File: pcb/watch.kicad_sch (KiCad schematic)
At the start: 18 parts, among them U1 nRF52840, Y1 Crystal

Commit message: sussy
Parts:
- added C17, C18: 12pF, symbol Device:C_Small
- added D10, D11, D9: D_TVS, symbol Device:D_TVS
- added F2: 1A/1.8A, Fuse:Fuse_1206_3216Metric_Pad1.42x1.75mm_HandSolder, symbol Device:Polyfuse_Small
- added J1: USB_C_Receptacle_USB2.0_14P, Connector_USB:USB_C_Receptacle_G-Switch_GT-USB-7010ASV, symbol Connector:USB_C_Receptacle_USB2.0_14P
- added L3: 10uH, symbol Device:L_Small
- added R17, R18: 5.1k, Resistor_SMD:R_0603_1608Metric_Pad0.98x0.95mm_HandSolder, symbol Device:R_Small
- added Y2: 32.768KHz, symbol Device:Crystal
- Y1: value Crystal -> 32MHz
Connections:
- net GND: now also C10.1, C11.1, C17.1, C18.1, D10.1 (A1), D11.1 (A1), D9.1 (A1), J1.A1 (GND), J1.A12 (GND), J1.B1 (GND), J1.B12 (GND), J1.S1 (SHIELD), R17.2, R18.2
- net VBUS: now also D11.2 (A2), F2.2
- net at C11.2: now also U1.A23 (XC2), Y1.1
- net at Y1.2: now also C10.2, U1.B24 (XC1)
- net VDD_nRF: now reaches C3.1, C4.1, C5.1, C6.1, C7.1, U1.A22 (VDD), U1.AD14 (VDD), U1.AD23 (VDD), U1.B1 (VDD), U1.W1 (VDD)
- net VDD_nRF: now also L3.1
- net at U1.AB2 (DCCH): now also L3.2
- net P0.16: now reaches U1.AC11 (P0.16)
- net P0.25: now reaches U1.AC21 (P0.25)
- net P0.14: now reaches U1.AC9 (P0.14)
- net P0.15: now reaches U1.AD10 (P0.15)
- net D-: now reaches U1.AD4 (D-)
- net D-: now also D10.2 (A2), J1.A7 (D-), J1.B7 (D-)
- net D+: now reaches U1.AD6 (D+)
- net D+: now also D9.2 (A2), J1.A6 (D+), J1.B6 (D+)
- net P0.13: now reaches U1.AD8 (P0.13)
- net at U1.D2 (XL1/P0.00): now also C18.2, Y2.1
- net at U1.F2 (XL2/P0.01): now also C17.2, Y2.2
- net P0.26: now reaches U1.G1 (P0.26)
- net P1.06: now reaches U1.R24 (P1.06)
- net P1.05: now reaches U1.T23 (P1.05)
- net P1.04: now reaches U1.U24 (P1.04)
- new net: J1.B5 (CC2), R18.1
- new net: J1.A5 (CC1), R17.1
- new net: F2.1, J1.A4 (VBUS), J1.A9 (VBUS), J1.B4 (VBUS), J1.B9 (VBUS)
- no-connect marks 5 -> 9
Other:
- moved on the sheet: C10, C11, C12, C13, C14, C15, C2, C3, C4, C5, C6, C7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

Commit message: stuff
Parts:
- added SW1, SW2, SW3, SW4: SW_Push, symbol Switch:SW_Push
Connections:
- net GND: now also SW1.2, SW2.2, SW3.2, SW4.2
- net P1.13: now reaches U1.A16 (P1.13)
- net P1.10: now reaches U1.A20 (P1.10)
- net P1.14: now reaches U1.B15 (P1.14)
- net P1.12: now reaches U1.B17 (P1.12)
- net P1.11: now reaches U1.B19 (P1.11)
- net P1.07: now reaches U1.P23 (P1.07)
- net P1.07: now also SW4.1
- net P1.03: now reaches U1.V23 (P1.03)
- net P1.03: now also SW3.1
- net P1.02: now reaches U1.W24 (P1.02)
- net P1.02: now also SW2.1
- net P1.01: now reaches U1.Y23 (P1.01)
- net P1.01: now also SW1.1
- no-connect marks 9 -> 14
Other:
- moved on the sheet: D10, D11, D9, F2, J1, R17, R18

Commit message: sus commit
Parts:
- removed D10, D11, D9: D_TVS, symbol Device:D_TVS
- added U9: USBLC6-2SC6, Package_TO_SOT_SMD:SOT-23-6, symbol Power_Protection:USBLC6-2SC6
- C10, C11, C17, C18: footprint (none) -> Capacitor_SMD:C_0402_1005Metric; LCSC Part (none) -> C1547
- C12: footprint (none) -> Capacitor_SMD:C_0402_1005Metric; LCSC Part (none) -> C52923
- C13: footprint (none) -> Capacitor_SMD:C_0603_1608Metric; LCSC Part (none) -> C1622
- C14: footprint (none) -> Capacitor_SMD:C_0402_1005Metric; LCSC Part (none) -> C1546
- C15, C7, C8, C9: footprint (none) -> Capacitor_SMD:C_0603_1608Metric; LCSC Part (none) -> C19666
- C2, C3, C4, C5, C6: footprint (none) -> Capacitor_SMD:C_0402_1005Metric; LCSC Part (none) -> C1525
- L1, L3: footprint (none) -> Inductor_SMD:L_0805_2012Metric; LCSC Part (none) -> C88182
- L2: footprint (none) -> Inductor_SMD:L_0402_1005Metric; LCSC Part (none) -> C98055
- R17, R18: value 5.1k -> 4.12k; footprint Resistor_SMD:R_0603_1608Metric_Pad0.98x0.95mm_HandSolder -> Resistor_SMD:R_0402_1005Metric; LCSC Part C23186 -> C2930007
- SW1, SW2, SW3, SW4: value SW_Push -> 10k; footprint (none) -> Resistor_SMD:R_0402_1005Metric; LCSC Part (none) -> C25744
- U1: value nRF52840 -> 5.1k; footprint Package_DFN_QFN:Nordic_AQFN-73-1EP_7x7mm_P0.5mm -> Resistor_SMD:R_0603_1608Metric_Pad0.98x0.95mm_HandSolder; LCSC Part (none) -> C23186
- Y1: value 32MHz -> RV-3028-C7; footprint (none) -> Package_SON:MicroCrystal_C7_SON-8_1.5x3.2mm_P0.9mm; LCSC Part (none) -> C3019759
- Y2: footprint (none) -> Package_TO_SOT_SMD:SOT-23-6; LCSC Part (none) -> C7519
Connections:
- net D+: now also U9.3 (I/O2)
- net D-: now also U9.1 (I/O1)
- net GND: now also U9.2 (GND)
- net VBUS: now also U9.5 (VBUS)
- net P0.23: now reaches U1.AC19 (P0.23)
- net TIMEPULSE: now reaches U1.AD12 (P0.17)
- net P0.27: now reaches U1.H2 (P0.27)
- no-connect marks 14 -> 16

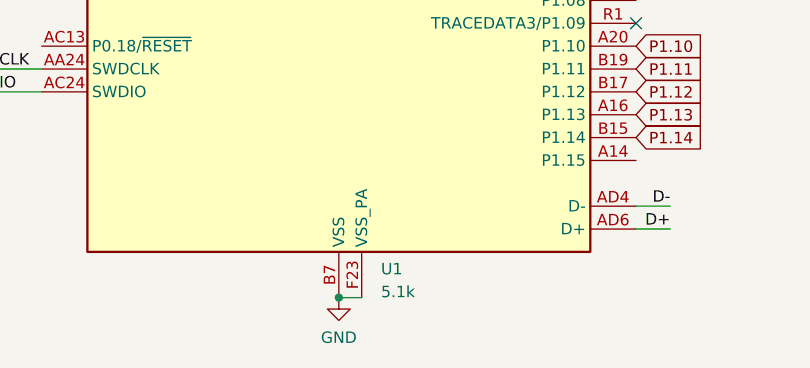
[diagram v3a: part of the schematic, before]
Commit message: fix symbols getting absolutely goofed up
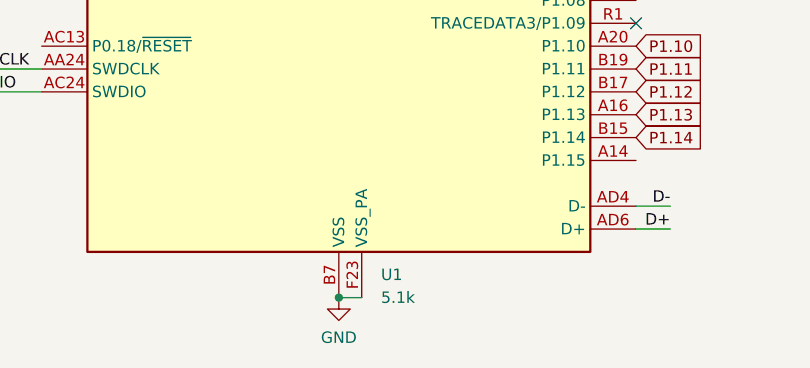
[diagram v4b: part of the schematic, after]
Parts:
- U1: footprint Resistor_SMD:R_0603_1608Metric_Pad0.98x0.95mm_HandSolder -> Package_DFN_QFN:Nordic_AQFN-73-1EP_7x7mm_P0.5mm
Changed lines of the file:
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@@
 		(fields_autoplaced yes)
 		(property "Reference" "U1"
-			(at 132.9533 187.325 0)
+			(at 132.9533 187.96 0)
 			(show_name no)
 			(do_not_autoplace no)
@@
 		)
 		(property "Value" "5.1k"
-			(at 132.9533 189.865 0)
+			(at 132.9533 190.5 0)
 			(show_name no)
 			(do_not_autoplace no)
@@
 			)
 		)
-		(property "Footprint" "Resistor_SMD:R_0603_1608Metric_Pad0.98x0.95mm_HandSolder"
+		(property "Footprint" "Package_DFN_QFN:Nordic_AQFN-73-1EP_7x7mm_P0.5mm"
 			(at 128.27 193.04 0)
 			(hide yes)
@@
 			)
 		)
-		(property "Datasheet" ""
+		(property "Datasheet" "http://infocenter.nordicsemi.com/topic/com.nordic.infocenter.nrf52/dita/nrf52/chips/nrf52840.html"
 			(at 111.76 71.12 0)
 			(hide yes)
@@
 			)
 		)
-		(property "Description" "Resistor, small symbol"
+		(property "Description" "Multiprotocol BLE/ANT/2.4 GHz/802.15.4 Cortex-M4F SoC, AQFN-73"
 			(at 128.27 119.38 0)
 			(hide yes)

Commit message: fix more stuffies
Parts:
- removed Y2: 32.768KHz, Package_TO_SOT_SMD:SOT-23-6, symbol Device:Crystal
- added Y3: 32MHz, Crystal:Crystal_SMD_2016-4Pin_2.0x1.6mm, symbol Device:Crystal_GND24
- SW1, SW2, SW3, SW4: value 10k -> SW_Push; footprint Resistor_SMD:R_0402_1005Metric -> (none); LCSC Part C25744 -> (none)
- U1: value 5.1k -> nRF52840
- Y1: value RV-3028-C7 -> 32.768KHz; footprint Package_SON:MicroCrystal_C7_SON-8_1.5x3.2mm_P0.9mm -> (none); LCSC Part C3019759 -> (none)
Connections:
- net GND: now also Y3.2 (G), Y3.4 (G)
- net at C11.2, U1.A23 (XC2): now also Y3.3; no longer Y1.1
- net at C10.2, U1.B24 (XC1): now also Y3.1; no longer Y1.2
- net at C18.2, U1.D2 (XL1/P0.00): now also Y1.2
- net at C17.2, U1.F2 (XL2/P0.01): now also Y1.1

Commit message: ALMOST done with parts purgatory
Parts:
- C17, C18: value 12pF -> 22pF; LCSC Part C1547 -> C1555
- U9: LCSC Part (none) -> C7519
- Y1: LCSC Part (none) -> C32346
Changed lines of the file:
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@@
 			)
 		)
+		(property "LCSC Part" "C32346"
+			(at 180.34 57.15 0)
+			(hide yes)
+			(show_name no)
+			(do_not_autoplace no)
+			(effects
+				(font
+					(size 1.27 1.27)
+				)
+			)
+		)
 		(pin "1"
 		)
@@
 			)
 		)
+		(property "LCSC Part" "C7519"
+			(at 265.43 69.85 0)
+			(hide yes)
+			(show_name no)
+			(do_not_autoplace no)
+			(effects
+				(font
+					(size 1.27 1.27)
+				)
+			)
+		)
 		(pin "4"
 		)
@@
 			)
 		)
-		(property "Value" "12pF"
+		(property "Value" "22pF"
 			(at 196.596 47.752 90)
 			(show_name no)
@@
 			)
 		)
-		(property "LCSC Part" "C1547"
+		(property "LCSC Part" "C1555"
 			(at 196.85 53.34 90)
 			(hide yes)
@@
 			)
 		)
-		(property "Value" "12pF"
+		(property "Value" "22pF"
 			(at 196.85 64.008 90)
 			(show_name no)
@@
 			)
 		)
-		(property "LCSC Part" "C1547"
+		(property "LCSC Part" "C1555"
 			(at 196.85 60.96 90)
 			(hide yes)

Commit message: sussy
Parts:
- removed C17, C18: 22pF, Capacitor_SMD:C_0402_1005Metric, symbol Device:C_Small
- removed Y1: 32.768KHz, symbol Device:Crystal
- renumbered C3 to C1, C7 to C10, C8 to C11, C15 to C12, C12 to C13, C13 to C14, C9 to C2, C10 to C3, C11 to C4, C14 to C5, C4 to C6, C2 to C7, C5 to C8, C6 to C9, F2 to F1, L3 to L1, L1 to L2, L2 to L3, R17 to R1, R18 to R2, U9 to U2, Y3 to Y1
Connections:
- net GND: now also J1.SH (SHIELD), U1.F2 (XL2/P0.01); no longer J1.S1 (SHIELD)
- net LF_EXT_CLK: now reaches U1.D2 (XL1/P0.00)

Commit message: amogus
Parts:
- SW1, SW2, SW3, SW4: now not fitted; now left out of the parts list
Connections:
- net P1.15: now reaches U1.A14 (P1.15)
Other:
- moved on the sheet: C1, C10, C11, C12, C13, C14, C2, C3, C4, C5, C6, C7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
